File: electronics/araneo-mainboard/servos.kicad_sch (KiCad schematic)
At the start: 16 parts, among them J1 Servo1, J2 Servo2, J3 Servo3, J4 Servo4, J5 Servo5, J6 Servo7, J7 Servo6, J8 Servo8

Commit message: electronics: assign footprints
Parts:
- C1, C2, C3, C4, C5, C6, C7, C8: footprint (none) -> PCM_JLCPCB:C_0402
- J1, J2, J3, J4, J5, J6, J7, J8: footprint (none) -> Connector_PinHeader_2.54mm:PinHeader_1x03_P2.54mm_Vertical
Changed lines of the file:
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@@
 			)
 		)
-		(property "Footprint" ""
+		(property "Footprint" "Connector_PinHeader_2.54mm:PinHeader_1x03_P2.54mm_Vertical"
 			(at 179.07 140.97 0)
 			(hide yes)
@@
 			)
 		)
-		(property "Footprint" ""
+		(property "Footprint" "Connector_PinHeader_2.54mm:PinHeader_1x03_P2.54mm_Vertical"
 			(at 179.07 39.37 0)
 			(hide yes)
@@
 			)
 		)
-		(property "Footprint" ""
+		(property "Footprint" "PCM_JLCPCB:C_0402"
 			(at 108.9152 119.38 0)
 			(hide yes)
@@
 			)
 		)
-		(property "Footprint" ""
+		(property "Footprint" "Connector_PinHeader_2.54mm:PinHeader_1x03_P2.54mm_Vertical"
 			(at 179.07 106.68 0)
 			(hide yes)
@@
 			)
 		)
-		(property "Footprint" ""
+		(property "Footprint" "Connector_PinHeader_2.54mm:PinHeader_1x03_P2.54mm_Vertical"
 			(at 127 39.37 0)
 			(hide yes)
@@
 			)
 		)
-		(property "Footprint" ""
+		(property "Footprint" "PCM_JLCPCB:C_0402"
 			(at 160.9852 153.67 0)
 			(hide yes)
@@
 			)
 		)
-		(property "Footprint" ""
+		(property "Footprint" "PCM_JLCPCB:C_0402"
 			(at 160.9852 86.36 0)
 			(hide yes)
@@
 			)
 		)
-		(property "Footprint" ""
+		(property "Footprint" "PCM_JLCPCB:C_0402"
 			(at 160.9852 52.07 0)
 			(hide yes)
@@
 			)
 		)
-		(property "Footprint" ""
+		(property "Footprint" "PCM_JLCPCB:C_0402"
 			(at 108.9152 52.07 0)
 			(hide yes)
@@
 			)
 		)
-		(property "Footprint" ""
+		(property "Footprint" "Connector_PinHeader_2.54mm:PinHeader_1x03_P2.54mm_Vertical"
 			(at 127 73.66 0)
 			(hide yes)
@@
 			)
 		)
-		(property "Footprint" ""
+		(property "Footprint" "Connector_PinHeader_2.54mm:PinHeader_1x03_P2.54mm_Vertical"
 			(at 127 106.68 0)
 			(hide yes)
@@
 			)
 		)
-		(property "Footprint" ""
+		(property "Footprint" "PCM_JLCPCB:C_0402"
 			(at 108.9152 86.36 0)
 			(hide yes)
@@
 			)
 		)
-		(property "Footprint" ""
+		(property "Footprint" "Connector_PinHeader_2.54mm:PinHeader_1x03_P2.54mm_Vertical"
 			(at 179.07 73.66 0)
 			(hide yes)
@@
 			)
 		)
-		(property "Footprint" ""
+		(property "Footprint" "PCM_JLCPCB:C_0402"
 			(at 108.9152 153.67 0)
 			(hide yes)
@@
 			)
 		)
-		(property "Footprint" ""
+		(property "Footprint" "PCM_JLCPCB:C_0402"
 			(at 160.9852 119.38 0)
 			(hide yes)
@@
 			)
 		)
-		(property "Footprint" ""
+		(property "Footprint" "Connector_PinHeader_2.54mm:PinHeader_1x03_P2.54mm_Vertical"
 			(at 127 140.97 0)
 			(hide yes)

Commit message: electronics: update bom
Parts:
- J1, J2, J3, J4, J5, J6, J7, J8: now left out of the parts list
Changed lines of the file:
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@@
 		(body_style 1)
 		(exclude_from_sim no)
-		(in_bom yes)
+		(in_bom no)
 		(on_board yes)
 		(in_pos_files yes)
@@
 		(body_style 1)
 		(exclude_from_sim no)
-		(in_bom yes)
+		(in_bom no)
 		(on_board yes)
 		(in_pos_files yes)
@@
 		(body_style 1)
 		(exclude_from_sim no)
-		(in_bom yes)
+		(in_bom no)
 		(on_board yes)
 		(in_pos_files yes)
@@
 		(body_style 1)
 		(exclude_from_sim no)
-		(in_bom yes)
+		(in_bom no)
 		(on_board yes)
 		(in_pos_files yes)
@@
 		(body_style 1)
 		(exclude_from_sim no)
-		(in_bom yes)
+		(in_bom no)
 		(on_board yes)
 		(in_pos_files yes)
@@
 		(body_style 1)
 		(exclude_from_sim no)
-		(in_bom yes)
+		(in_bom no)
 		(on_board yes)
 		(in_pos_files yes)
@@
 		(body_style 1)
 		(exclude_from_sim no)
-		(in_bom yes)
+		(in_bom no)
 		(on_board yes)
 		(in_pos_files yes)
@@
 		(body_style 1)
 		(exclude_from_sim no)
-		(in_bom yes)
-		(on_board yes)
-		(in_pos_files yes)
+		(in_bom no)
+		(on_board yes)
+		(in_pos_files yes)

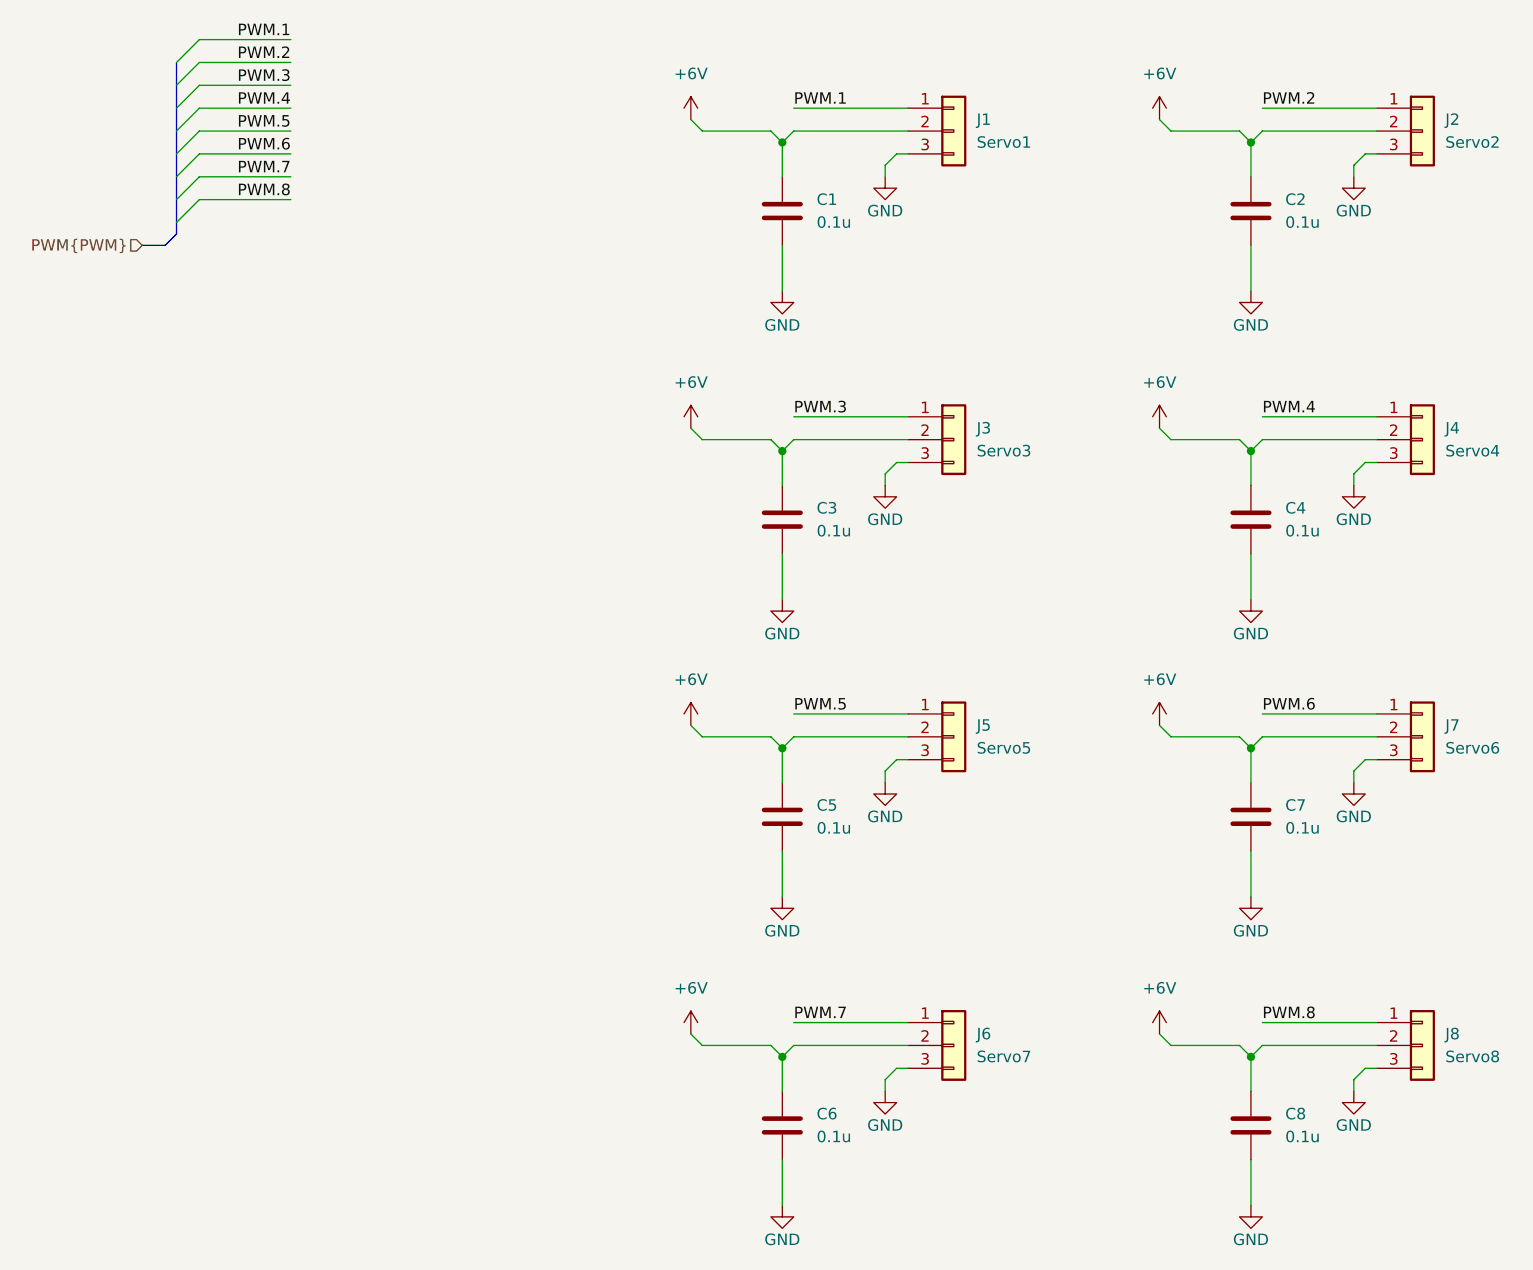
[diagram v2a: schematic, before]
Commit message: improve schematic and layout, add LCSC parts
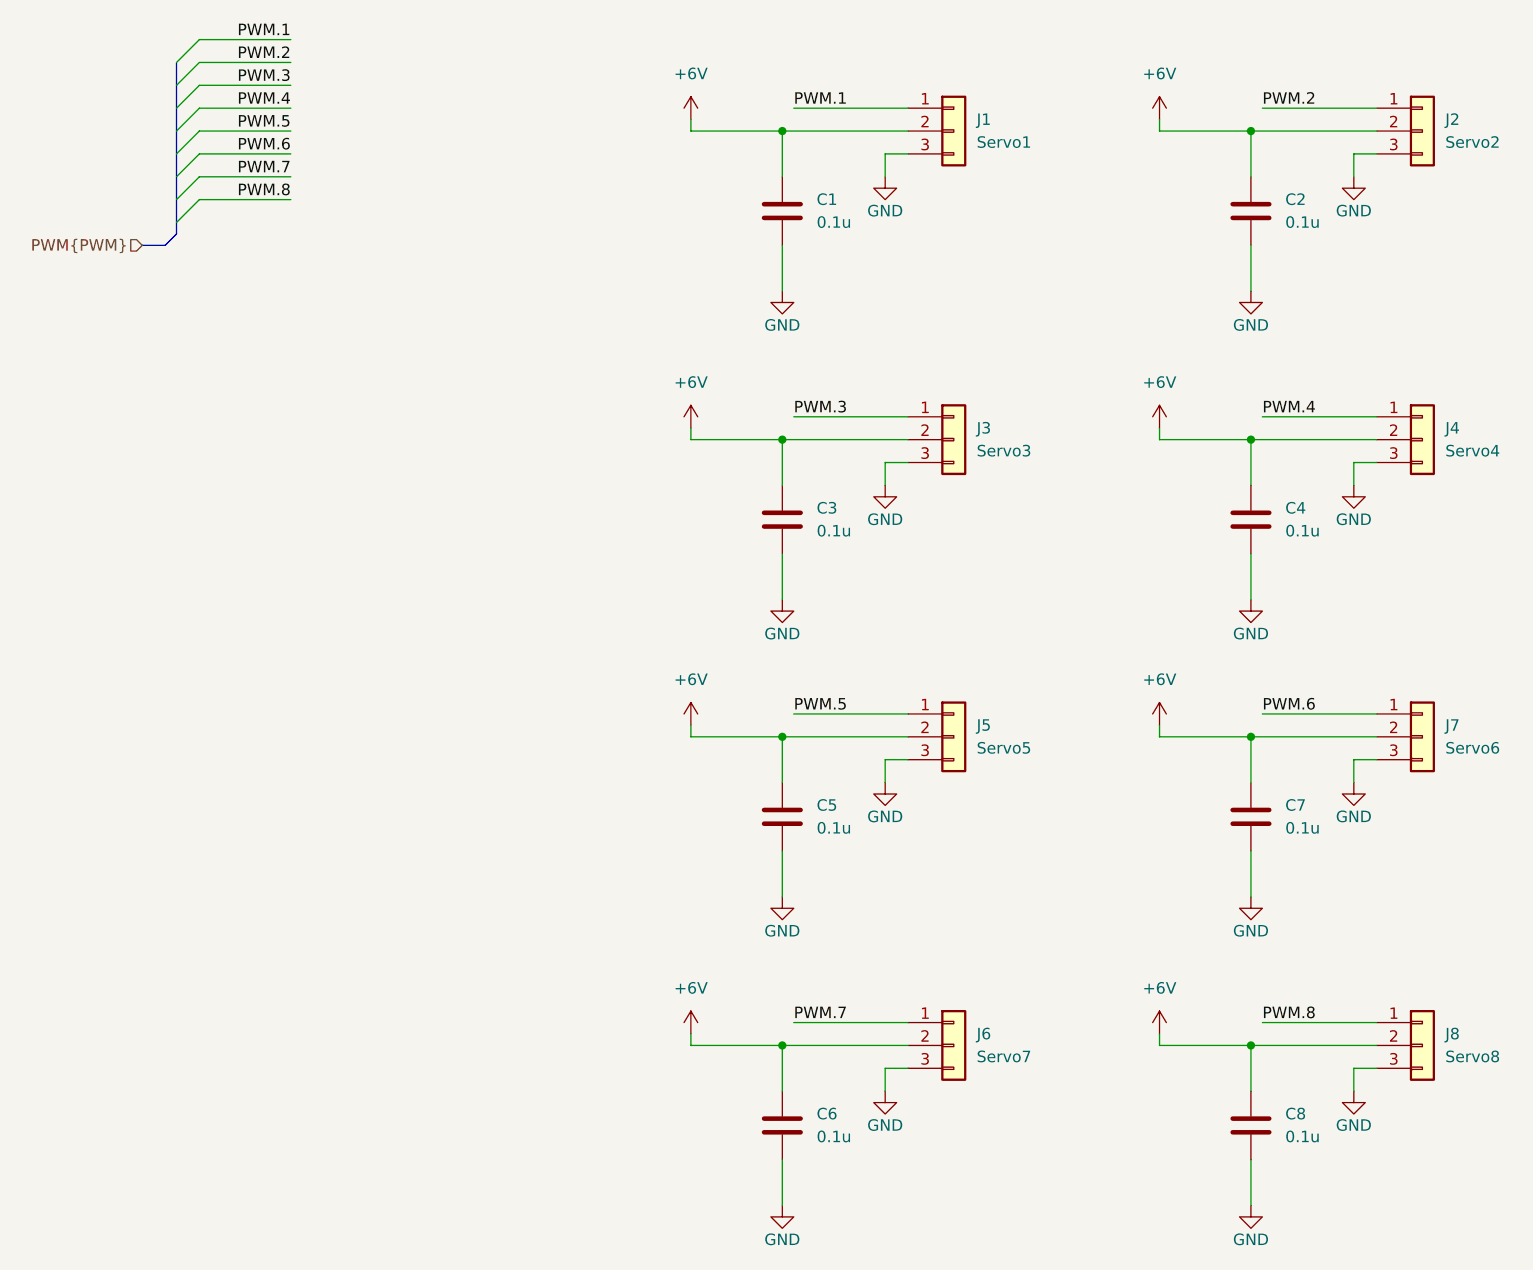
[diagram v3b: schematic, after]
